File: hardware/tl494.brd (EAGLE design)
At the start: 100 x 80 mm, 79 parts, among them IC1 TL494CN, J1 CON_HEADER_1X02-PTH, K2 24V, Q1 2N5551, Q1I 8050, Q1I1 2N3904, Q2 8550, Q2I 8050, Q3 8050, Q4 2SK4145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

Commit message: minor updates on board
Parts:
- added H1, H2, H3, H4: MOUNT-PAD-ROUND3.3, holes:3,3-PAD
- added T2, T4: PAD_TERMINAL-1.02MM_ROUND, dp_devices.v6:CON_PAD_ROUND_1.02MM
- moved R22 15.2 mm to (59.7, 2.54)
- moved Q1I1 10.2 mm to (62.2, 11.4)
- moved D4 9.92 mm to (91.4, 47.0)
- moved C7 8.03 mm to (61.0, 36.8)
- moved C11 7.92 mm to (82.3, 53.3)
- moved D9 7.73 mm to (16.5, 76.2)
- moved D5 7.73 mm to (59.7, 43.2)
- moved Q3 6.84 mm to (63.5, 26.7)
- moved C8 6.84 mm to (61.0, 31.8)
- moved Q2 6.84 mm to (58.4, 26.7)
- moved R10 6.84 mm to (30.5, 63.5)
- moved R9 6.84 mm to (22.9, 58.4)
- moved R18 6.48 mm to (72.4, 43.2)
- moved R6 6.48 mm to (34.3, 63.5)
- moved C9 6.35 mm to (52.1, 54.6)
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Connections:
- net GND: now also T4.P
- net VOUT: now also T2.P

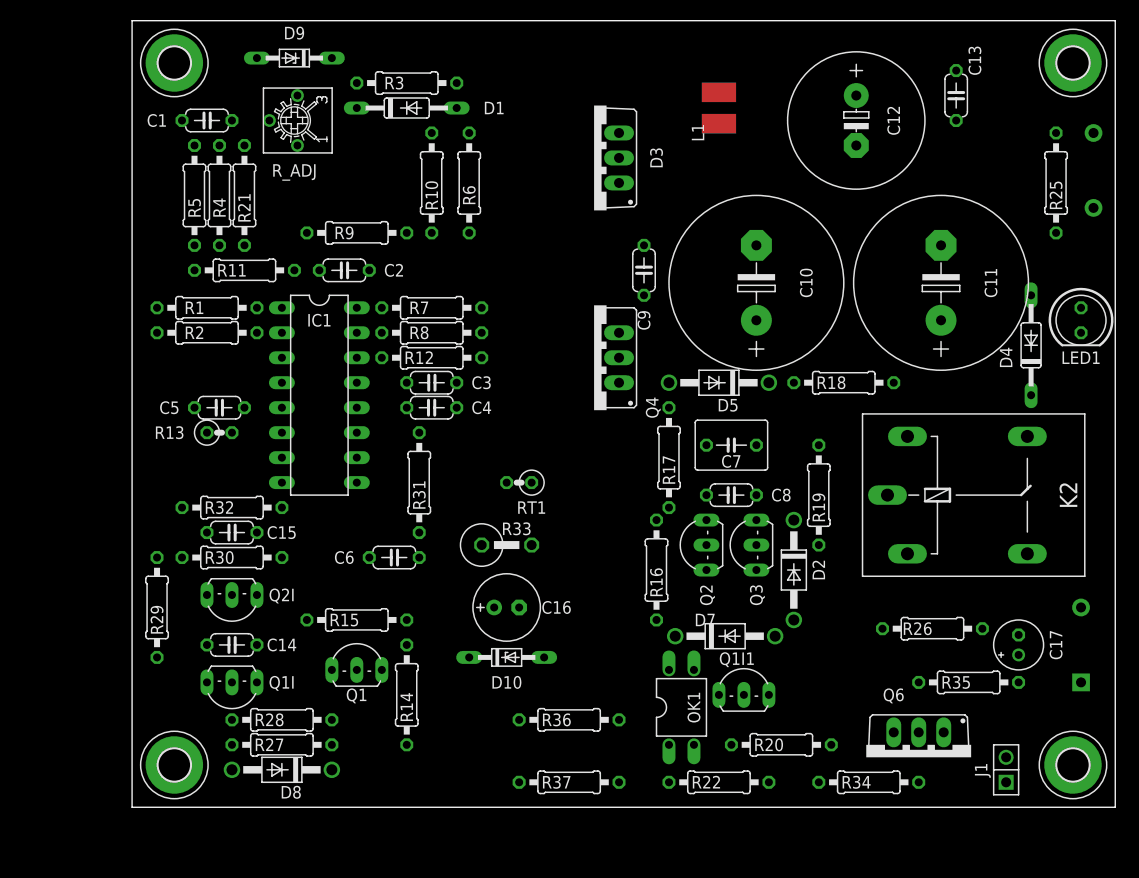
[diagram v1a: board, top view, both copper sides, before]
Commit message: fix spice latch circuit, started routing
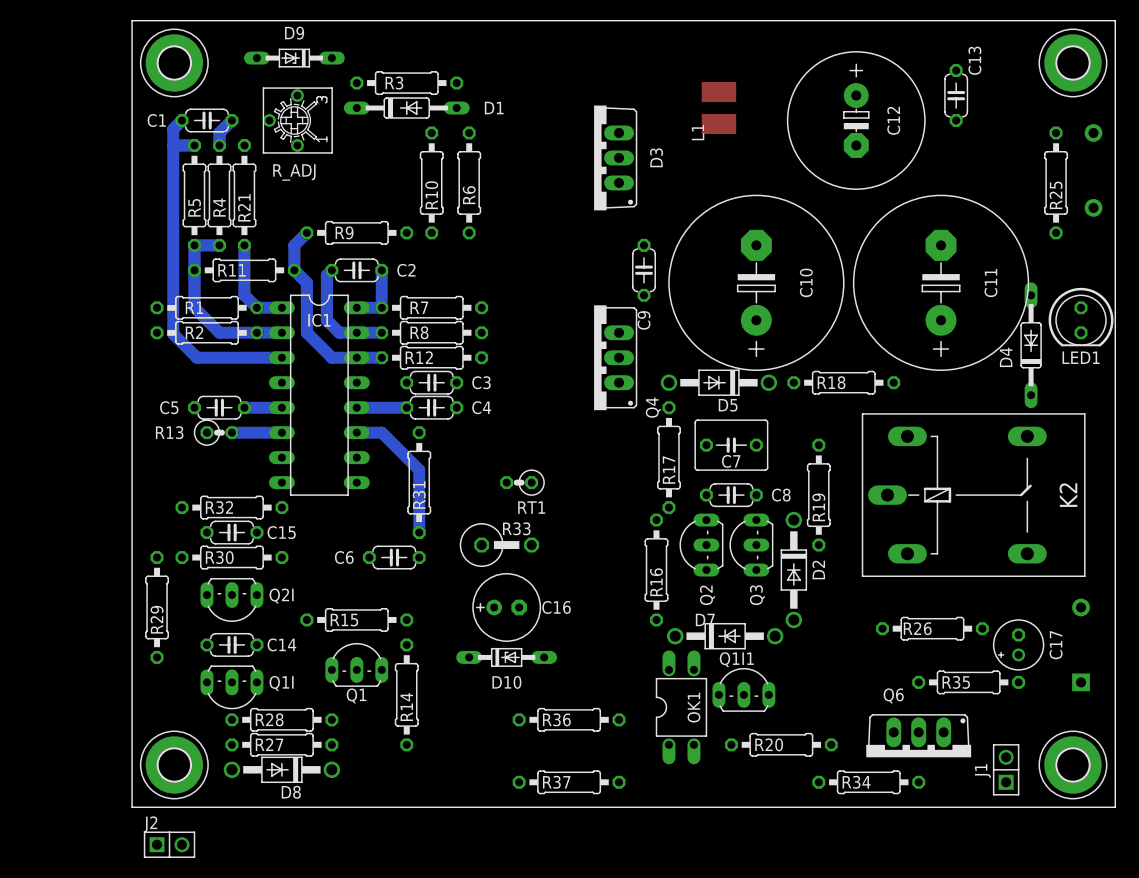
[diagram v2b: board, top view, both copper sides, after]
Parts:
- removed R22: 1K, rcl:0207/10
- added J2: CON_HEADER_1X02-PTH, dp_devices.v6:M1X2
- C10, C11: value 1000uF 50V -> 1000uF 63V
- R20: value 1K -> 10K
- moved C2 1.27 mm to (22.9, 54.6)
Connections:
- new net N$29: J2.1, OK1.4
- net GND: no longer OK1.2
- net N$20: now also OK1.1, R20.2; no longer Q1I1.2, R20.1
- net N$33: now also Q1I1.2; no longer R20.2, R22.2
- net N$34: now also OK1.2
- net N$35: now also J2.2, OK1.3; no longer OK1.1, R22.1
- net VIN: now also R20.1
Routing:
- net N$6: track 0.00 -> 36.3 mm
- net VREF: track 0.00 -> 19.9 mm
- net N$4: track 0.00 -> 18.8 mm
- net N$10: track 0.00 -> 14.3 mm
- net N$8: track 0.00 -> 11.4 mm
- net N$7: track 0.00 -> 9.42 mm
- net N$1: track 0.00 -> 6.35 mm
- net +15V: track 0.00 -> 5.08 mm
- net N$12: track 0.00 -> 5.08 mm
- net N$11: track 0.00 -> 3.81 mm
- net N$5: track 0.00 -> 3.07 mm

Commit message: done board routing
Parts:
- removed H3, H4: MOUNT-PAD-ROUND3.3, holes:3,3-PAD
- removed L1: INDUCTOR-L1812, dp_devices.v6:L1812
- added J3: J20MM, jumper:20
- added J4: J5MM, jumper:05
- added J5: J15MM, jumper:15
- added L2: (no value), rcl:TJ5-U1
- added R22: 560R 1W, trosh_devices.eagle.v9:0414V_EXPAD
- C1, C13, C14, C15, C2, C3, C4, C5, C6, C8, C9: device rcl:C050-024X044 -> trosh_devices.eagle.v9:C050-024X044_EXPAD
- C16: device rcl:E2,5-7 -> trosh_devices.eagle.v9:E2,5-7_EXPAD
- C17: device rcl:E2-5 -> trosh_devices.eagle.v9:E2-5_EXPAD
- C7: device rcl:C050-050X075 -> trosh_devices.eagle.v9:C050-050X075_EXPAD
- R1, R10, R11, R12, R15, R16, R2, R20, R25, R27, R28, R29, R3, R30, R31, R6, R7, R8, R9: device rcl:0207/10 -> trosh_devices.eagle.v9:0207/10_EXPAD
- R13: device rcl:0207/2V -> trosh_devices.eagle.v9:0207/2V_EXPAD
- R14, R17, R21, R32, R34, R35, R4, R5: device rcl:0207/10 -> trosh_devices.eagle.v9:0207/2V_EXPAD
- R18, R19: device rcl:0207/10 -> trosh_devices.eagle.v9:0414V_EXPAD
- R26: value 560*x2 1W -> 560R 1W; device rcl:0207/10 -> trosh_devices.eagle.v9:0414V_EXPAD
- R33: device rcl:0414V -> trosh_devices.eagle.v9:0414V_EXPAD
- R36: device rcl:0207/10 -> rcl:0207/2V
- RT1: value (none) -> RESISTOR0207/2V_EXPAD; device rcl:0207/2V -> trosh_devices.eagle.v9:0207/2V_EXPAD
- R_ADJ: device dp_devices.v6:TRIMMER_3362P -> trosh_devices.eagle.v9:TRIMMER_3362P_EXPAD
- moved H1 96.9 mm to (94.4, 40.0)
- moved J2 36.1 mm to (39.4, 2.54), turned to 180 degrees
- moved H2 35.8 mm to (6.21, 40.0)
- moved C17 33.4 mm to (57.1, 11.4)
- moved R37 33.0 mm to (77.5, 1.91), turned to 180 degrees
- moved R36 30.6 mm to (74.9, 6.35), turned to 90 degrees
- moved J1 24.1 mm to (64.8, 3.81), turned to 180 degrees
- moved D10 19.4 mm to (34.3, 34.3), turned to 90 degrees
- moved D4 18.3 mm to (74.3, 53.3)
- moved C13 14.8 mm to (97.2, 66.0)
- moved R35 14.6 mm to (70.5, 13.3), turned to 0 degrees
- moved C12 14.0 mm to (87.6, 69.8)
- moved R14 13.0 mm to (30.5, 24.1), turned to 0 degrees
- moved D1 12.0 mm to (21.6, 61.0)
- moved R3 11.7 mm to (20.3, 64.8)
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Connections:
- new net N$36: R22.2, R26.1
- new net N$37: D3.C, J3.2, L2.2
- new net N$38: J3.1, J4.1, Q4.3
- net +15V: now also R33.2; no longer R33.1
- net +V: now also R33.1; no longer R33.2
- net GND: now also J5.1, J5.2
- net N$17: now also J4.2; no longer D3.C, L1.1, Q4.3
- net N$18: now also R18.2; no longer R18.1
- net N$19: now also R18.1; no longer R18.2
- net N$22: now also R26.2; no longer R26.1
- net N$32: now also R22.1; no longer R26.2
- net VOUT: now also L2.1; no longer L1.2
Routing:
- net VOUT: track 0.00 -> 164.3 mm
- net N$24: track 0.00 -> 122.0 mm
- net N$23: track 0.00 -> 83.1 mm
- net N$14: track 0.00 -> 56.3 mm
- net N$28: track 0.00 -> 51.9 mm
- net +V: track 0.00 -> 46.9 mm
- net N$9: track 0.00 -> 39.9 mm
- net GND: track 0.00 -> 32.9 mm
- net N$16: track 0.00 -> 29.4 mm
- net N$18: track 0.00 -> 27.0 mm
- net N$34: track 0.00 -> 26.8 mm
- net +15V: track 5.08 -> 30.6 mm
- net VIN: track 0.00 -> 24.3 mm
- net N$15: track 0.00 -> 22.4 mm
- net N$33: track 0.00 -> 21.8 mm
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- added copper zone on layer 16, net +V
- added copper zone on layer 16, net GND
- added copper zone on layer 16, net N$37
- added copper zone on layer 16, net N$38
- added copper zone on layer 16, net VIN
- added copper zone on layer 16, net VOUT
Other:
- board text added: "01-08-2020"
- board text added: "LEADTECH CSPG 48V DC-DC MODULE V1.0"
